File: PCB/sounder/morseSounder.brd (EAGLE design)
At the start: 56.6 x 82.7 mm, 84 parts, among them IC1 LM386M-1, IC5 LM321MF, J1 AVR_SPI_PRG_6PTH, J2 POWERPOLE_POWER25A_HORIZONTAL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, J3 POWER_JACKPTH, Q1 MMBT3904, Q2 MMBT3904, Q3 MMBT3904, Q4 2.5A/30V/105mΩ, Q5 MMBT3904, T1 MMBTA42, U1 ATMEGA328P_TQFP

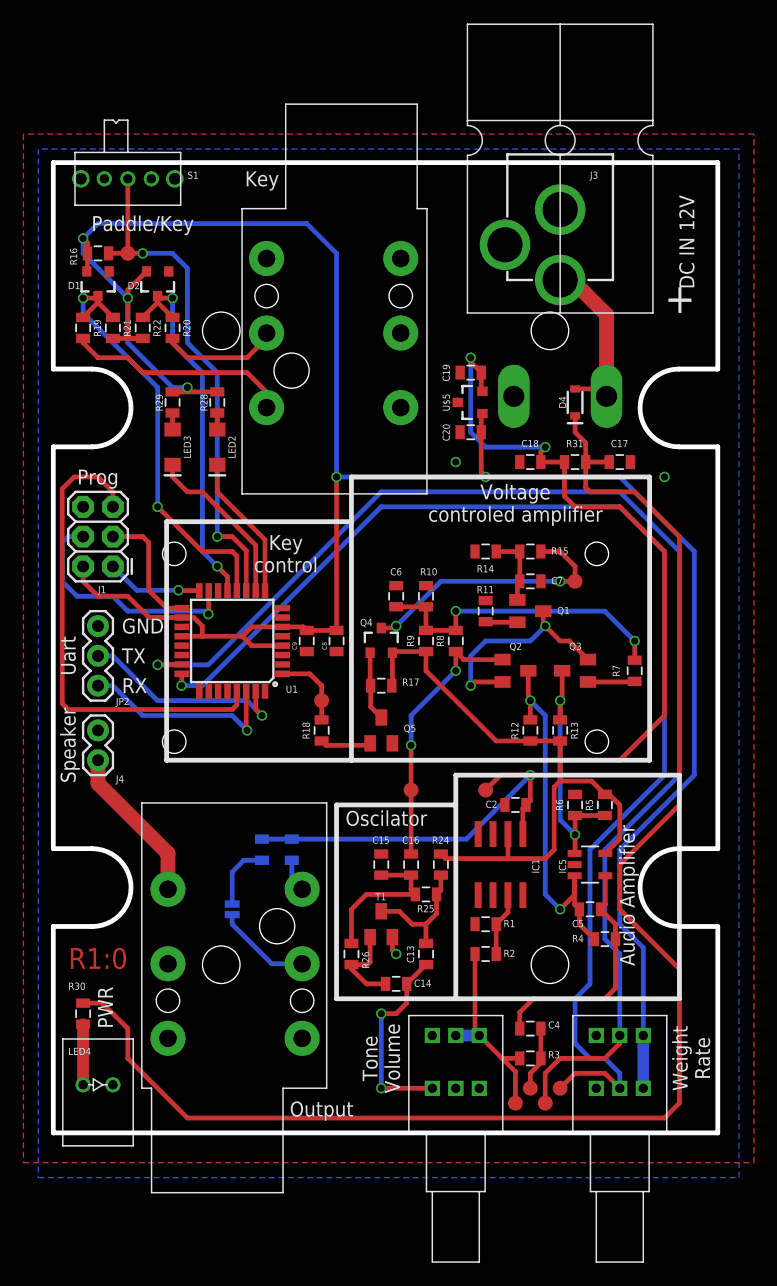
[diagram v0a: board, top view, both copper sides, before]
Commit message: Rebuilt audio circuit to use a synthesised digital source rather than a tone generator.
Other improvements.

RGB power light/status indicator.
Better amplifier circuit.
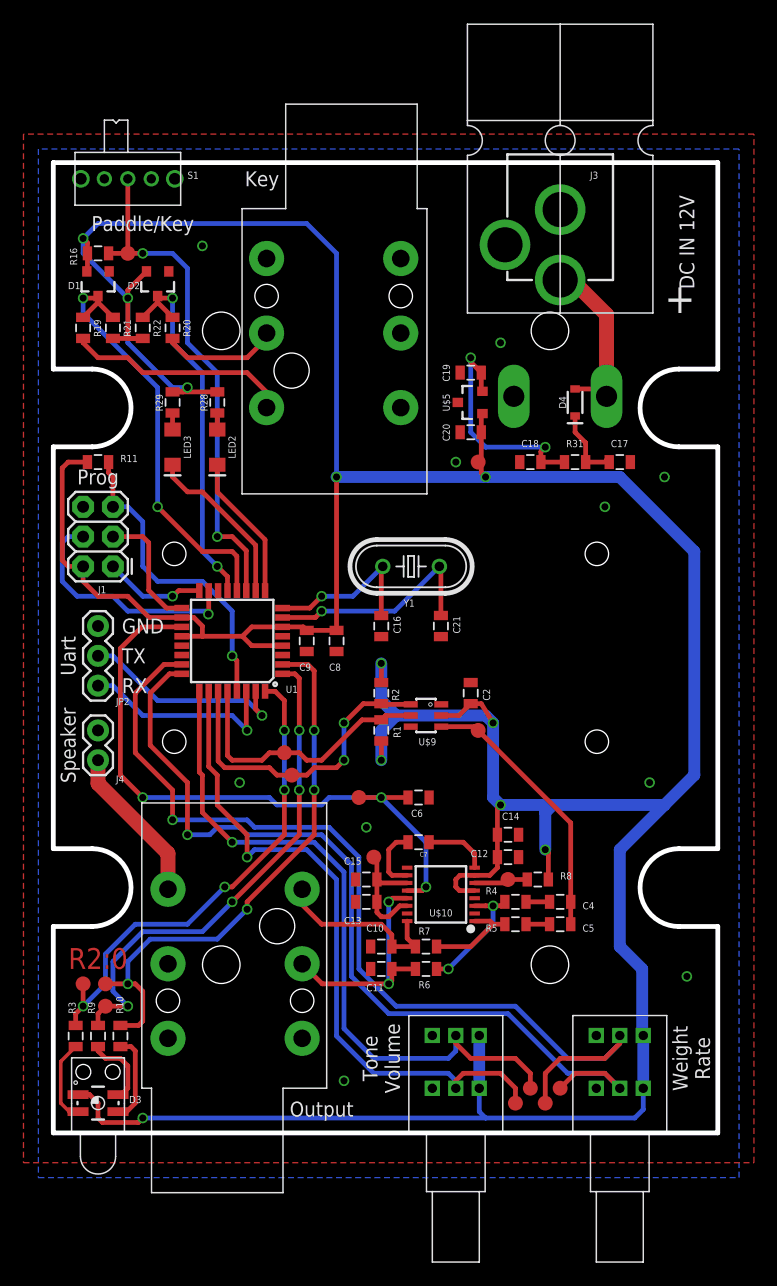
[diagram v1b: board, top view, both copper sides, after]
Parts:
- removed C1, C3: 100u, SparkFun:0805
- removed IC1: LM386M-1, linear:SO08
- removed IC5: LM321MF, linear:SOT23-5
- removed LED4: LED-902118128, morseSounder:MULTICOMP-2118128
- removed Q1, Q2, Q3, Q5: MMBT3904, transistor:SOT23-BEC
- removed Q4: 2.5A/30V/105mΩ, SparkFun-DiscreteSemi:SOT23-3
- removed R12, R13, R14, R15, R30: 22K, SparkFun:0805
- removed R17, R18: 10K, SparkFun:0805
- removed R24: 4.7K, SparkFun:0805
- removed R25, R26: 18K, SparkFun:0805
- removed SJ1: SOLDERJUMPERNO, SparkFun:SJ_2S-NO
- removed T1: MMBTA42, SparkFun:SOT23
- added C10, C11: 1n, SparkFun:0805
- added C12: 1u, SparkFun:0805
- added C21: 22p, SparkFun:0805
- added D3: RGB, morseSounder:P-LCC-4-3
- added TP10, TP11, TP12, TP13, TP14, TP15: TEST-POINT3X5, SparkFun-Connectors:PAD.03X.05
- added U$10: MAX13331, morseSounder:SSOP16
- added U$8: SLP3SLP3, morseSounder:SLP-3
- added U$9: DAC_MCP4725SOT, SparkFun:SOT23-6
- added Y1: (no value), SparkFun:HC49U-V
- C13: value 0.018u -> 1u
- C14: value 0.018u -> 100n
- C15: value 0.047u -> 100n
- C16: value 0.047u -> 22p
- C2: value 200n -> 1u
- C4: value 100n -> 330n
- C5: value 10n -> 330n
- C6: value 100u -> 1n
- C7: value 100n -> 1u
- R1: value 1K -> 10K
- R10, R3, R9: value 10K -> 330
- R11: value 22K -> 10K
- R2: value 15K -> 10K
- R4, R5: value 10K -> 30K
- R6: value 10K -> 45K
- R7: value 330 -> 45K
- R8: value 330 -> 10K
- moved R10 45.6 mm to (5.71, 8.26), turned to 270 degrees
- moved R9 43.7 mm to (3.81, 8.26), turned to 270 degrees
- moved R3 38.8 mm to (1.91, 8.26), turned to 270 degrees
- moved R11 35.4 mm to (3.81, 57.1), turned to 0 degrees
- moved TP8 31.9 mm to (36.2, 34.3)
- moved R7 29.5 mm to (31.8, 15.9), turned to 0 degrees
- moved TP7 29.2 mm to (20.3, 30.5)
- moved TP4 25.7 mm to (40.6, 3.81)
- moved C7 24.2 mm to (31.1, 24.8)
- moved R2 23.9 mm to (27.9, 37.5), turned to 90 degrees
- moved R8 21.5 mm to (41.3, 21.6), turned to 0 degrees
- moved C16 20.5 mm to (27.9, 43.2)
- moved R6 18.9 mm to (31.8, 14.0), turned to 0 degrees
- moved R1 18.8 mm to (27.9, 34.3), turned to 270 degrees
- moved C6 17.3 mm to (31.1, 28.6), turned to 0 degrees
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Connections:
- removed net AUDIO_OUT: C1.1, C2.1, C3.1, IC1.5, TP4.P$1
- removed net AUDIO_PRE_AMP: C4.2, R3.1, TP5.P$1
- removed net AVR_KEY_OUT: R18.1, TP9.P$1, U1.1
- removed net KEY_IN: Q4.3, R15.2, TP7.P$1
- removed net N$11: Q3.B, R7.2
- removed net N$12: C6.2, R10.1, R7.1, R8.2, R9.2
- removed net N$13: Q1.E, R11.2
- removed net N$14: SJ1.2, U$2.P$5
- removed net N$24: C14.1, R26.1, T1.1
- removed net N$25: C15.1, C16.1, R25.1, R26.2
- removed net N$26: C13.1, C14.2, U$3.F1
- removed net N$36: LED4.P$1, R30.1
- removed net N$9: C7.2, Q1.B, R14.2, R15.1
- new net ADC_MAX13331_DIAG: C6.1, TP12.P$1, U$10.12, U1.19
- new net ADC_TONE: TP5.P$1, U$3.F2, U1.26
- new net ADC_VOLUME: TP4.P$1, U$3.R2, U1.25
- new net LED_FRONT_BLU: R9.1, TP14.P$1, U1.1
- new net LED_FRONT_GRN: R10.1, TP15.P$1, U1.2
- new net LED_FRONT_RED: R3.1, TP13.P$1, U1.32
- new net N$19: D3.2, R3.2
- new net N$20: R8.1, TP11.P$1, U$10.6
- new net OUT_L: C10.1, R7.1, U$10.16, U$2.P$6
- new net OUT_R: C11.1, R6.1, U$10.13, U$2.P$5
- new net SCL: R1.1, TP6.P$1, U$9.5, U1.28
- new net SDA: R2.1, TP7.P$1, U$9.6, U1.27
- net +12V: no longer IC1.6, IC5.5, Q4.2, R12.1, R13.1, R17.2, R24.1, R5.1, R9.1
- net AVR_RESET: now also R11.2
- net AVR_VCC: now also C12.1, C14.1, C2.2, D3.1, R1.2, R11.1, R2.2, R8.2, TP10.P$1, U$10.5, U$10.7, U$3.F3, U$3.R3, U$9.2
- net GND: now also C10.2, C11.2, C12.2, C13.2, C14.2, C16.1, C2.1, C21.1, C6.2, U$10.15, U$10.2, U$10.4, U$10.9, U$3.F1, U$9.1, U$9.4; no longer C2.2, C6.1, C7.1, IC1.2, IC1.4, IC5.2, LED4.P$2, Q5.E, R1.1, R10.2, R11.1, R14.1, R6.2, T1.2, U$3.F2
- net N$1: now also C21.2, U1.7, Y1.2; no longer C3.2, U$2.P$6
- net N$15: now also D3.4, R9.2; no longer R2.2, R3.2, TP8.P$1, U$3.R2, U$3.R3
- net N$16: now also C7.1, U$10.8; no longer Q5.B, R18.2
- net N$17: now also C7.2, U$10.10; no longer Q4.1, Q5.C, R17.1
- net N$2: now also C16.2, U1.8, Y1.1; no longer C1.2, SJ1.1
- net N$23: now also C13.1, C15.1, TP9.P$1, U$10.11, U$10.14; no longer C13.2, R24.2, R25.2, T1.3
- net N$3: now also D3.3, R10.2; no longer IC1.3, R1.2, R2.1
- net N$4: no longer R30.2
- net N$5: now also C4.2, R4.2; no longer C4.1, C5.2, IC5.4, R4.1
- net N$6: now also C5.2, R5.2; no longer C5.1, IC5.3, Q2.C, R12.2, R4.2
- net N$7: now also R4.1, R6.2, U$10.3; no longer IC5.1, Q3.C, R13.2, R5.2, R6.1
- net N$8: now also R5.1, R7.2, U$10.1; no longer Q1.C, Q2.E, Q3.E
- net TONE_OUT: now also C4.1, C5.1, TP8.P$1, U$9.3; no longer C16.2, Q2.B, R8.1, TP6.P$1
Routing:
- net AVR_VCC: track 209.9 -> 348.4 mm, vias 5 -> 11
- net N$4: track 127.9 -> 6.64 mm
- net +12V: track 111.3 -> 19.9 mm
- net ADC_VOLUME: track 0.00 -> 59.4 mm, vias 0 -> 1
- net ADC_TONE: track 0.00 -> 57.9 mm, vias 0 -> 1
- net ADC_MAX13331_DIAG: track 0.00 -> 55.4 mm, vias 0 -> 3
- net LED_FRONT_GRN: track 0.00 -> 47.5 mm, vias 0 -> 4
- net LED_FRONT_BLU: track 0.00 -> 43.4 mm, vias 0 -> 4
- net LED_FRONT_RED: track 0.00 -> 41.9 mm, vias 0 -> 4
- net AUDIO_OUT: track 34.7 -> 0.00 mm, vias 1 -> 0
- net ADC_RATE: track 107.4 -> 74.8 mm
- net N$6: track 32.5 -> 2.01 mm, vias 2 -> 0
- net ADC_WEIGHT: track 109.7 -> 81.0 mm
- net SDA: track 0.00 -> 27.2 mm, vias 0 -> 2
- net N$12: track 26.7 -> 0.00 mm, vias 2 -> 0
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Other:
- board text added: "R2:0"
- board text removed: "Audio Amplifier"
- board text removed: "Key control"
- board text removed: "Oscilator"
- board text removed: "PWR"
- board text removed: "R1:0"
- board text removed: "Voltage controled amplifier"

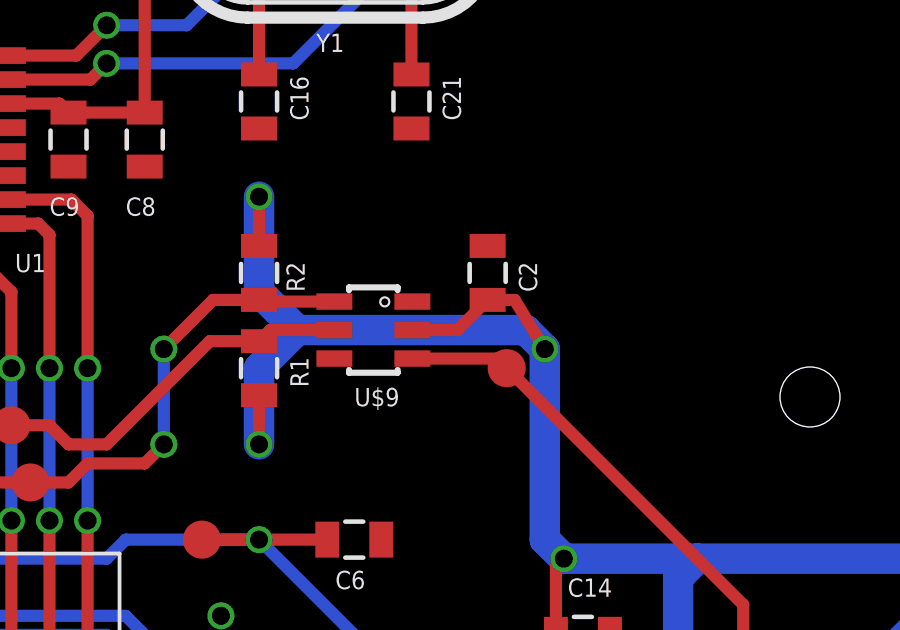
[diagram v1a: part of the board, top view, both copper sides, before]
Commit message: Fixed Pinout of DAC chip
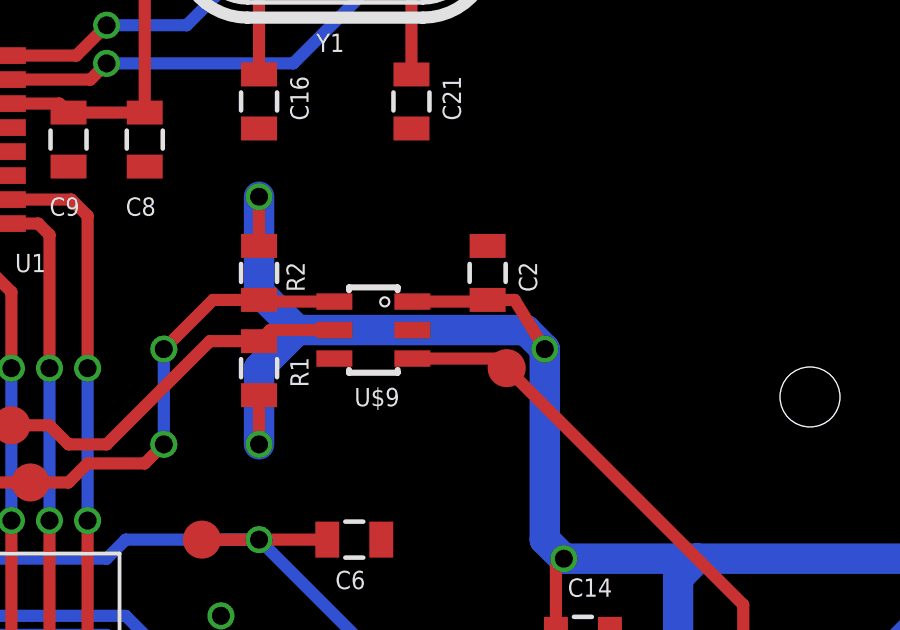
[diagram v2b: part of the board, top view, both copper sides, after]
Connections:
- net AVR_VCC: now also U$9.1; no longer U$9.2
- net GND: now also U$9.2; no longer U$9.1
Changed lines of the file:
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@@
 <?xml version="1.0" encoding="utf-8"?>
 <!DOCTYPE eagle SYSTEM "eagle.dtd">
-<eagle version="6.5.0">
+<eagle version="9.1.3">
 <drawing>
 <settings>
 <setting alwaysvectorfont="no"/>
+<setting keepoldvectorfont="yes"/>
 <setting verticaltext="up"/>
 </settings>
@@
 <param name="dpMaxLengthDifference" value="10mm"/>
 <param name="dpGapFactor" value="2.5"/>
-<param name="checkGrid" value="0"/>
 <param name="checkAngle" value="0"/>
 <param name="checkFont" value="1"/>
 <param name="checkRestrict" value="0"/>
+<param name="checkStop" value="0"/>
+<param name="checkValues" value="0"/>
+<param name="checkNames" value="1"/>
+<param name="checkWireStubs" value="1"/>
+<param name="checkPolygonWidth" value="0"/>
 <param name="useDiameter" value="13"/>
 <param name="maxErrors" value="50"/>
@@
 <pass name="Default">
 <param name="RoutingGrid" value="50mil"/>
+<param name="AutoGrid" value="1"/>
+<param name="Efforts" value="0"/>
+<param name="TopRouterVariant" value="1"/>
 <param name="tpViaShape" value="round"/>
 <param name="PrefDir.1" value="|"/>
@@
 </element>
 <element name="LED2" library="SparkFun-LED" package="LED-1206" value="" x="13.97" y="58.42" smashed="yes" rot="R270">
+<attribute name="NAME" x="14.9225" y="58.42" size="0.6096" layer="25" font="vector" rot="R270" align="bottom-center"/>
 <attribute name="PROD_ID" value="DIO-09912" x="13.97" y="58.42" size="1.778" layer="27" rot="R270" display="off"/>
+<attribute name="VALUE" x="13.0175" y="58.42" size="0.6096" layer="27" font="vector" ratio="20" rot="R270" align="top-center"/>
 <attribute name="VALUE" value="RED" x="13.97" y="58.42" size="1.778" layer="27" rot="R270" display="off"/>
-<attribute name="NAME" x="14.9225" y="58.42" size="0.6096" layer="25" font="vector" rot="R270" align="bottom-center"/>
-<attribute name="VALUE" x="13.0175" y="58.42" size="0.6096" layer="27" font="vector" ratio="20" rot="R270" align="top-center"/>
 </element>
 <element name="LED3" library="SparkFun-LED" package="LED-1206" value="" x="10.16" y="58.42" smashed="yes" rot="R270">
+<attribute name="NAME" x="11.1125" y="58.42" size="0.6096" layer="25" font="vector" rot="R270" align="bottom-center"/>
 <attribute name="PROD_ID" value="DIO-09912" x="10.16" y="58.42" size="1.778" layer="27" rot="R270" display="off"/>
+<attribute name="VALUE" x="9.2075" y="58.42" size="0.6096" layer="27" font="vector" ratio="20" rot="R270" align="top-center"/>
 <attribute name="VALUE" value="RED" x="10.16" y="58.42" size="1.778" layer="27" rot="R270" display="off"/>
-<attribute name="NAME" x="11.1125" y="58.42" size="0.6096" layer="25" font="vector" rot="R270" align="bottom-center"/>
-<attribute name="VALUE" x="9.2075" y="58.42" size="0.6096" layer="27" font="vector" ratio="20" rot="R270" align="top-center"/>
 </element>
 <element name="R29" library="SparkFun" package="0805" value="330" x="10.16" y="62.23" smashed="yes" rot="R90">
@@
 <element name="TP3" library="SparkFun-Connectors" package="PAD.03X.05" value="TEST-POINT3X5" x="6.35" y="74.93" rot="R90"/>
 <element name="D1" library="SparkFun-DiscreteSemi" package="SOT23-3" value="200mA/70V" x="3.81" y="72.39" smashed="yes" rot="R180">
+<attribute name="NAME" x="1.778" y="71.882" size="0.6096" layer="25" font="vector" align="bottom-center"/>
 <attribute name="PROD_ID" value="DIO-10647" x="3.81" y="72.39" size="1.778" layer="27" rot="R180" display="off"/>
-<attribute name="NAME" x="1.778" y="71.882" size="0.6096" layer="25" font="vector" align="bottom-center"/>
 <attribute name="VALUE" x="2.159" y="72.39" size="0.6096" layer="27" font="vector" ratio="20" rot="R270" align="top-center"/>
 </element>
 <element name="D2" library="SparkFun-DiscreteSemi" package="SOT23-3" value="200mA/70V" x="8.89" y="72.39" smashed="yes" rot="R180">
+<attribute name="NAME" x="6.858" y="71.882" size="0.6096" layer="25" font="vector" align="bottom-center"/>
 <attribute name="PROD_ID" value="DIO-10647" x="8.89" y="72.39" size="1.778" layer="27" rot="R180" display="off"/>
-<attribute name="NAME" x="6.858" y="71.882" size="0.6096" layer="25" font="vector" align="bottom-center"/>
 <attribute name="VALUE" x="7.239" y="72.39" size="0.6096" layer="27" font="vector" ratio="20" rot="R270" align="top-center"/>
 </element>
 <element name="D4" library="SparkFun-DiscreteSemi" package="SOD-323" value="0.5A/40V/420mV" x="44.45" y="62.23" smashed="yes" rot="R90">
+<attribute name="NAME" x="43.688" y="62.23" size="0.6096" layer="25" font="vector" rot="R90" align="bottom-center"/>
 <attribute name="PROD_ID" value="DIO-10955" x="44.45" y="62.23" size="1.778" layer="27" rot="R90" display="off"/>
-<attribute name="NAME" x="43.688" y="62.23" size="0.6096" layer="25" font="vector" rot="R90" align="bottom-center"/>
 <attribute name="VALUE" x="45.212" y="62.23" size="0.6096" layer="27" font="vector" ratio="20" rot="R90" align="top-center"/>
 </element>
@@
 </element>
 <element name="U1" library="SparkFun-IC-Microcontroller" package="TQFP32-08" value="ATMEGA328P_TQFP" x="15.24" y="41.91" smashed="yes" rot="R180">
+<attribute name="NAME" x="20.32" y="38.1" size="0.6096" layer="25" font="vector" rot="R180" align="bottom-center"/>
 <attribute name="PROD_ID" value="IC-09069" x="15.24" y="41.91" size="1.778" layer="27" rot="R180" display="off"/>
-<attribute name="NAME" x="20.32" y="38.1" size="0.6096" layer="25" font="vector" rot="R180" align="bottom-center"/>
 <attribute name="VALUE" x="15.24" y="48.26" size="0.6096" layer="27" font="vector" ratio="20" rot="R180" align="bottom-center"/>
 </element>
@@
 <contactref element="U$3" pad="F1"/>
 <contactref element="U$3" pad="R1"/>
-<contactref element="U$9" pad="1"/>
 <contactref element="C2" pad="1"/>
 <contactref element="U$10" pad="2"/>
@@
 <via x="53.975" y="13.335" extent="1-16" drill="0.6"/>
 <via x="26.67" y="26.035" extent="1-16" drill="0.6"/>
+<contactref element="U$9" pad="2"/>
 </signal>
 <signal name="+12V">
@@
 <contactref element="R1" pad="2"/>
 <contactref element="R2" pad="2"/>
-<contactref element="U$9" pad="2"/>
 <contactref element="C2" pad="2"/>
 <contactref element="TP10" pad="P$1"/>
@@
 <wire x1="48.26" y1="15.875" x2="50.165" y2="13.97" width="1.016" layer="16"/>
 <wire x1="50.165" y1="13.97" x2="50.165" y2="8.255" width="1.016" layer="16"/>
-<wire x1="33.0501" y1="35.56" x2="34.555" y2="35.56" width="0.4064" layer="1"/>
-<wire x1="34.555" y1="35.56" x2="35.56" y2="36.565" width="0.4064" layer="1"/>
 <wire x1="35.56" y1="36.565" x2="36.46" y2="36.565" width="0.4064" layer="1"/>
 <wire x1="36.46" y1="36.565" x2="37.465" y2="34.925" width="0.4064" layer="1"/>
@@
 <via x="7.62" y="1.27" extent="1-16" drill="0.6"/>
 <wire x1="7.62" y1="1.27" x2="36.83" y2="1.27" width="0.4064" layer="16"/>
+<contactref element="U$9" pad="1"/>
+<wire x1="33.0501" y1="36.51" x2="35.505" y2="36.51" width="0.4064" layer="1"/>
+<wire x1="35.505" y1="36.51" x2="35.56" y2="36.565" width="0.4064" layer="1"/>
 <wire x1="50.26" y1="8.3" x2="50.165" y2="8.255" width="0" layer="19" extent="16-16"/>
 </signal>
@@
 </signal>
 </signals>
+<mfgpreviewcolors>
+<mfgpreviewcolor name="soldermaskcolor" color="0xC8008000"/>
+<mfgpreviewcolor name="silkscreencolor" color="0xFFFEFEFE"/>
+<mfgpreviewcolor name="backgroundcolor" color="0xFF282828"/>
+<mfgpreviewcolor name="coppercolor" color="0xFFFFBF00"/>
+<mfgpreviewcolor name="substratecolor" color="0xFF786E46"/>
+</mfgpreviewcolors>
 <errors>
 </errors>
